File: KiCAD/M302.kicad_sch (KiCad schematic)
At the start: 33 parts, among them J1 I2C-SHT3x, J10 To J3, J11 To J9, J12 DIN-3, J13 To Datalogger, J2 I2C-ThmCp, J3 I2C-3, J4 I2C-4, J5 I2C-D400, J6 W5500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

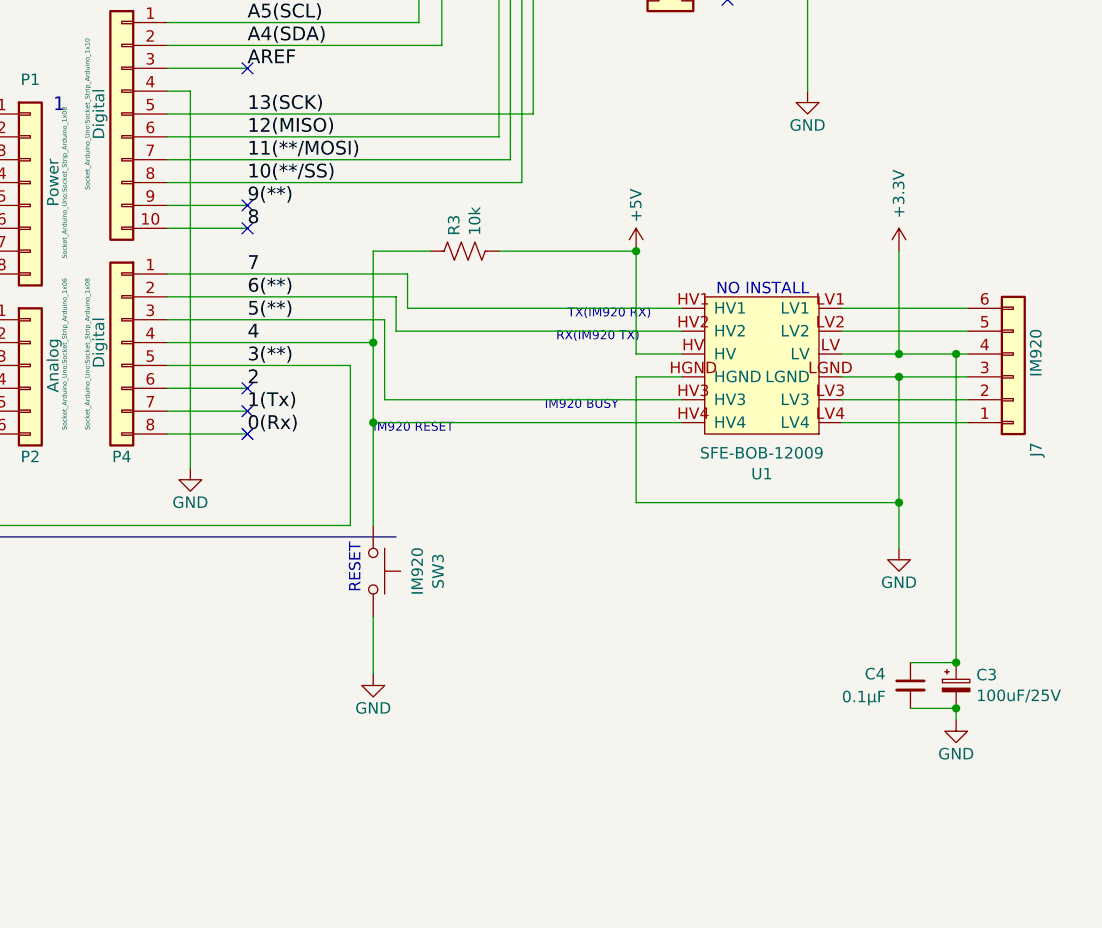
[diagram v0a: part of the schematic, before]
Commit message: CAD: 不要な回路を削除
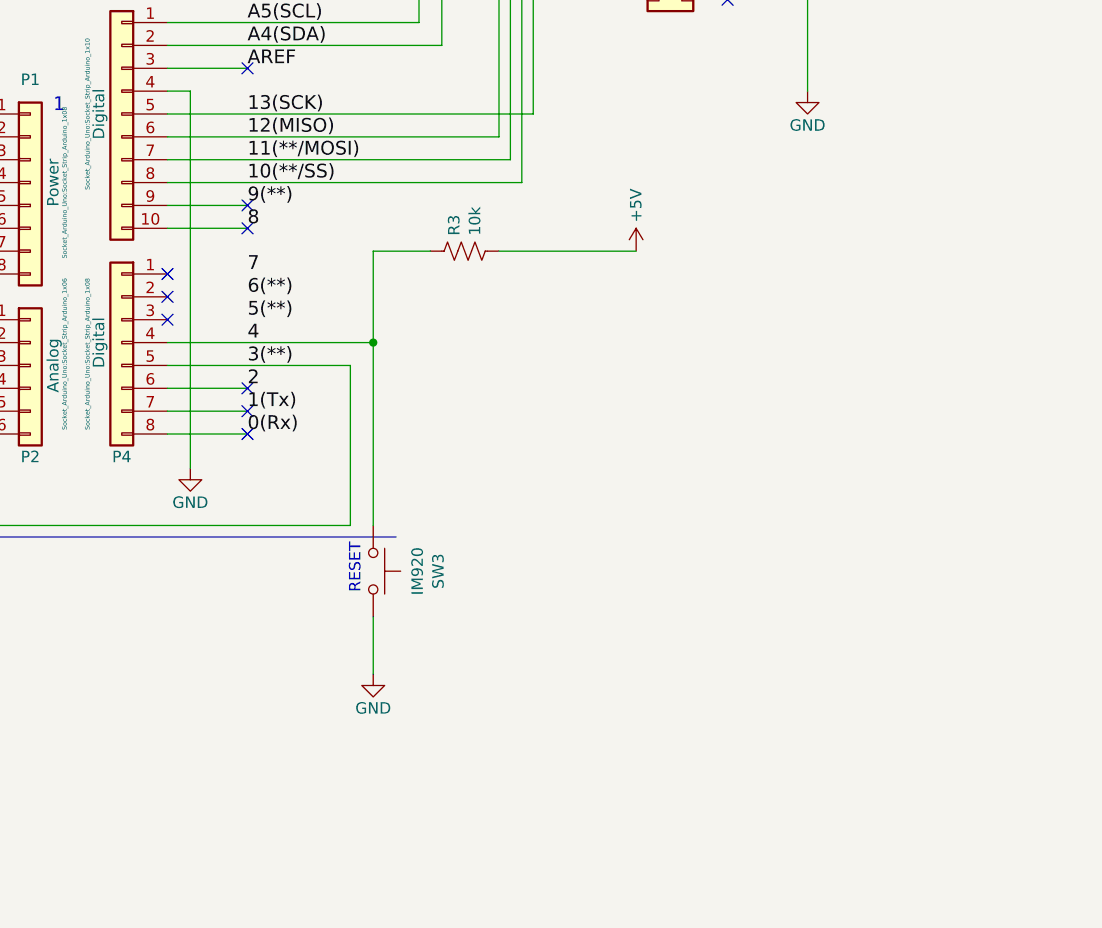
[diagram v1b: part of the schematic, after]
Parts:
- removed C3: 100uF/25V, Capacitor_THT:CP_Radial_D5.0mm_P2.00mm, symbol M302-rescue:CP_Small-Device
- removed C4: 0.1μF, Capacitor_THT:C_Disc_D3.0mm_W2.0mm_P2.50mm, symbol Device:C_Small
- removed J7: IM920, Connector_JST:JST_XH_B6B-XH-A_1x06_P2.50mm_Vertical, symbol Connector_Generic:Conn_01x06
- removed U1: SFE-BOB-12009, HOLLY:SFE-BOB-12009, symbol Buffer:SFE-BOB-12009
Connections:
- net 5(**): no longer P4.3 (Pin_3)
- net 6(**): no longer P4.2 (Pin_2)
- net 7: no longer P4.1 (Pin_1)
- no-connect marks 25 -> 28
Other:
- note removed: "IM920 BUSY"
- note removed: "IM920 RESET"
- note removed: "NO INSTALL"
- note removed: "RX(IM920 TX)"
- note removed: "TX(IM920 RX)"
